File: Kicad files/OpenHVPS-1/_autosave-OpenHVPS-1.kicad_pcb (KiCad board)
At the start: 2 copper layers, 77.5 x 20.5 mm, 71 parts, among them J1 Conn_01x03_Male, J2 Conn_01x03_Male, Q1 FQT7N10, Q2 BC846, Q3 MMDT3906, U1 74HC14, U2 MAX4162, U3 CD14538BM, U4 MAX6008AEUR+T

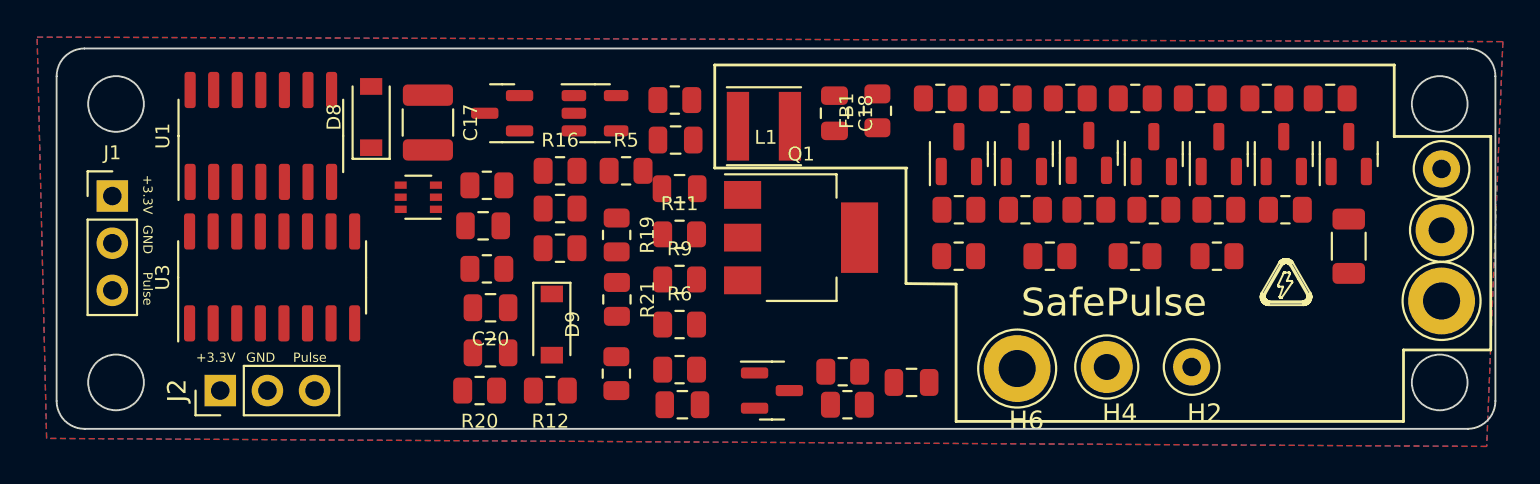
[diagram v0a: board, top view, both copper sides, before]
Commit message: Added extra outputs and A-C placement moved
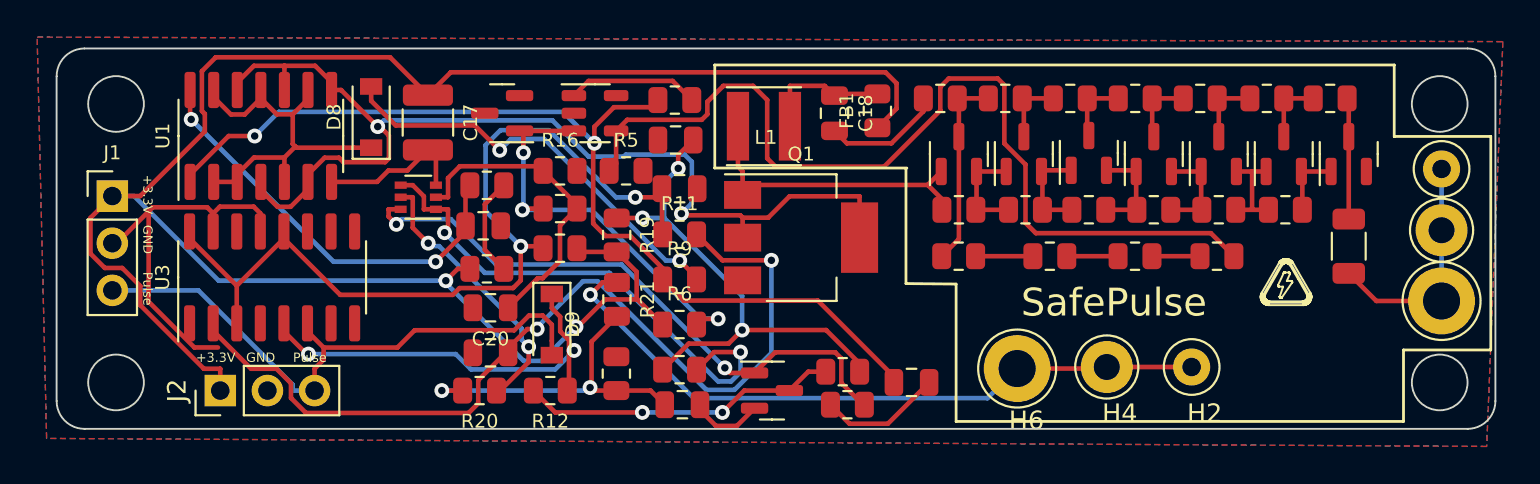
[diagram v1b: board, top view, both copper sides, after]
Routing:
- net +3V3: track 0.00 -> 108.9 mm, vias 0 -> 2
- net Net-(Q1-Pad2): track 0.00 -> 57.3 mm, vias 0 -> 2
- net Net-(C14-Pad1): track 0.00 -> 53.8 mm, vias 0 -> 2
- net Net-(R4-Pad1): track 0.00 -> 51.0 mm
- net Net-(C16-Pad1): track 0.00 -> 49.5 mm, vias 0 -> 2
- net Net-(C19-Pad1): track 0.00 -> 47.4 mm, vias 0 -> 2
- net GND: track 0.00 -> 45.9 mm
- net Net-(H2-Pad1): track 0.00 -> 37.1 mm, vias 0 -> 1
- net Net-(Q2-Pad1): track 0.00 -> 32.8 mm, vias 0 -> 2
- net Net-(D9-Pad2): track 0.00 -> 32.4 mm
- net Net-(Q3-Pad1): track 0.00 -> 28.1 mm, vias 0 -> 2
- net Net-(C21-Pad1): track 0.00 -> 27.9 mm, vias 0 -> 3
- net Net-(D9-Pad1): track 0.00 -> 23.2 mm, vias 0 -> 2
- net Net-(D8-Pad2): track 0.00 -> 22.8 mm, vias 0 -> 2
- net Net-(C15-Pad1): track 0.00 -> 22.8 mm, vias 0 -> 2
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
